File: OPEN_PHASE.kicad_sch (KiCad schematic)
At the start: 0 parts

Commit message: Rename the project to OPEN_PHASE
PhaseSense-8586 was named after the first parts of the design (INA240 +
ADS8586S), which are no longer on the board. OPEN_PHASE follows
OPEN_WEIGHT, the other OPEN THRUST LAB board.

- project files: OPEN_PHASE.kicad_pro / _sch / _pcb / _prl / _dru
- libraries: lib/lib_sym/OPEN_PHASE.kicad_sym and
  lib/lib_fp/OPEN_PHASE.pretty, nickname OPEN_PHASE in both tables, in
  every lib_id and in every footprint of the PCB
- project name of every symbol and sheet instance, so the reference
  designators are kept
- PROJECT_NAME and GIT_URL in the project and in kibot_main.yaml, README
  and its template, CHANGELOG, LTspice headers and their generator
- the README note now says the project was first published as
  PhaseSense-8586

The GitHub repository is now foukouda/OPEN_PHASE. The board name
PHASETRACKER is unchanged. The netlist, ERC and DRC reports are the same
before and after the rename.

Co-Authored-By: Claude Opus 5.5 <noreply@anthropic.com>
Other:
- title: PhaseSense-8586 - PHASETRACKER -> OPEN_PHASE - PHASETRACKER
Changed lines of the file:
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@@
 	(paper "A3")
 	(title_block
-		(title "PhaseSense-8586 - PHASETRACKER")
+		(title "OPEN_PHASE - PHASETRACKER")
 		(date "2026-10-06")
 		(rev "${REVISION}")
@@
 		)
 		(instances
-			(project "PhaseSense-8586"
+			(project "OPEN_PHASE"
 				(path "/f9e05184-c88b-4a88-ae9c-ab2bdb32be7c"
 					(page "9")
@@
 		)
 		(instances
-			(project "PhaseSense-8586"
+			(project "OPEN_PHASE"
 				(path "/f9e05184-c88b-4a88-ae9c-ab2bdb32be7c"
 					(page "10")
@@
 		)
 		(instances
-			(project "PhaseSense-8586"
+			(project "OPEN_PHASE"
 				(path "/f9e05184-c88b-4a88-ae9c-ab2bdb32be7c"
 					(page "2")
@@
 		)
 		(instances
-			(project "PhaseSense-8586"
+			(project "OPEN_PHASE"
 				(path "/f9e05184-c88b-4a88-ae9c-ab2bdb32be7c"
 					(page "3")

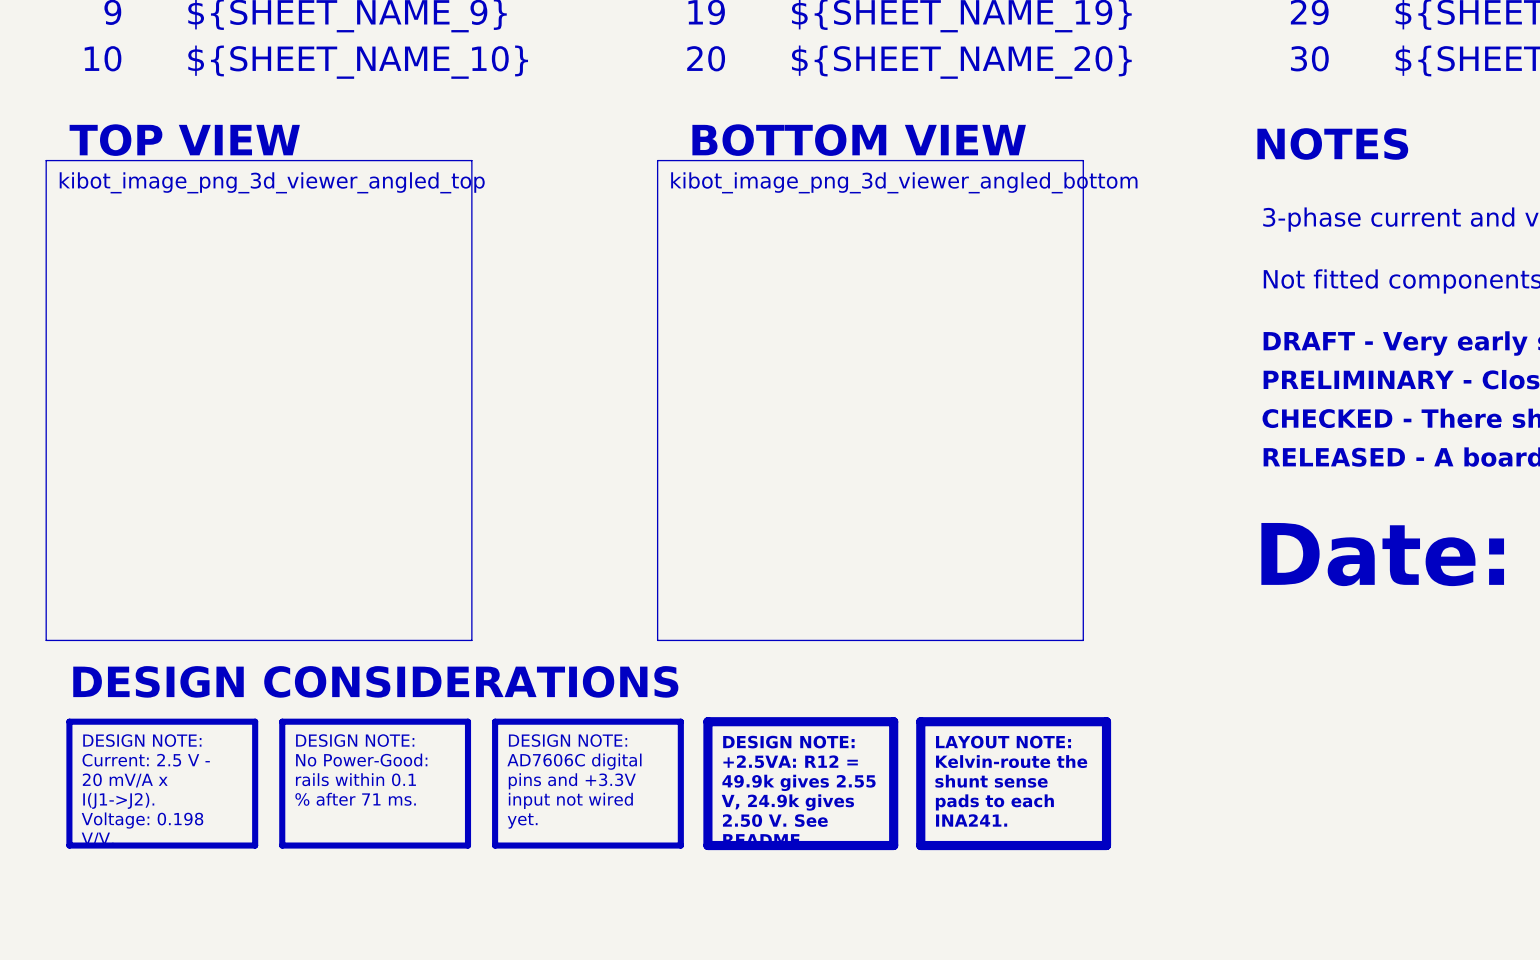
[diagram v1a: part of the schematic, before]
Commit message: Restyle schematic sheets, new title block logo, WE-MAPI inductor in simulations
- Schematic sheets: restyled frames, tables and text boxes
- Title block: INGENIERIE FRANCE logo in KDT_Template_GIT.kicad_wks
- LTspice: L1 modelled as WE-MAPI 4030 74438357022 (22 mOhm),
  simulations 01 and 03 rerun, README and results updated

Co-Authored-By: Claude Opus 5.5 <noreply@anthropic.com>
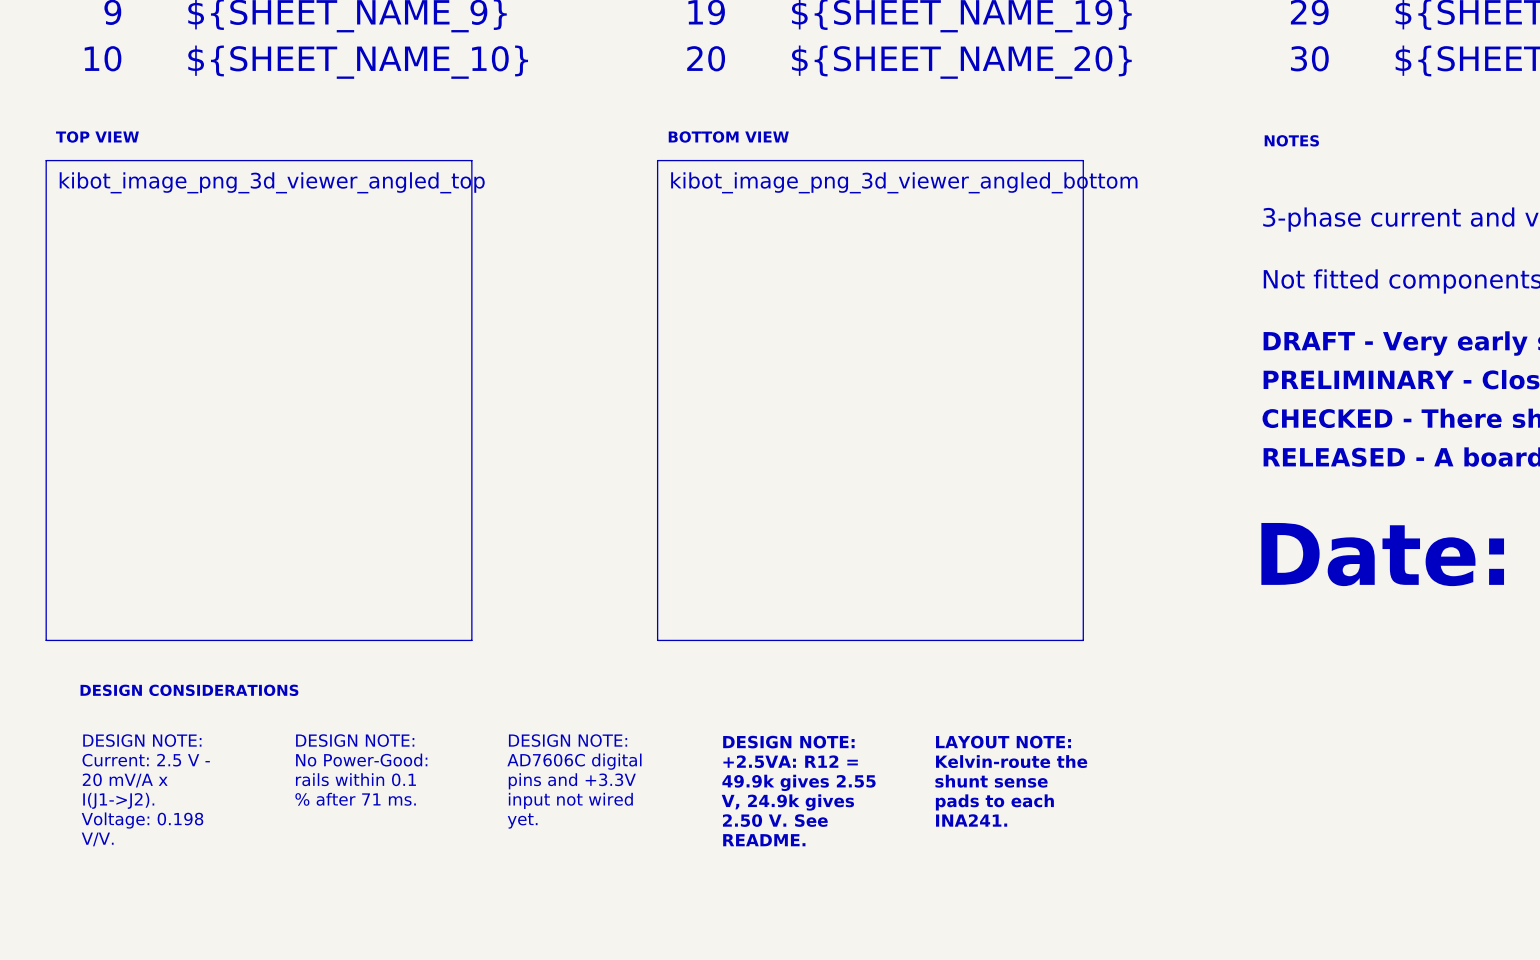
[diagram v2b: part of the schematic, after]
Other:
- note removed: "BOTTOM VIEW"
- note removed: "DESIGN CONSIDERATIONS"
- note removed: "NOTES"
- note removed: "TOP VIEW"
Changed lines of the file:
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@@
-		)
-	)
-	(text "BOTTOM VIEW"
-		(exclude_from_sim no)
-		(at 128.27 166.37 0)
-		(effects
-			(font
-				(face "Arial")
-				(size 5 5)
-				(bold yes)
-				(color 53 60 207 1)
-			)
-			(justify left bottom)
 		)
 	)
@@
 		)
 	)
-	(text "NOTES"
-		(exclude_from_sim no)
-		(at 220.98 167.005 0)
-		(effects
-			(font
-				(face "Arial")
-				(size 5 5)
-				(bold yes)
-				(color 53 60 207 1)
-			)
-			(justify left bottom)
-		)
-	)
 	(text "${SHEET_NAME_40}"
 		(exclude_from_sim no)
@@
 		)
 	)
-	(text "TOP VIEW"
-		(exclude_from_sim no)
-		(at 26.67 166.37 0)
-		(effects
-			(font
-				(face "Arial")
-				(size 5 5)
+	(text "34"
+		(exclude_from_sim no)
+		(at 332.74 106.68 0)
+		(effects
+			(font
+				(face "Times New Roman")
+				(size 4 4)
+				(color 0 0 0 1)
+			)
+			(justify right bottom)
+			(href "#34")
+		)
+	)
+	(text "${SHEET_NAME_10}"
+		(exclude_from_sim no)
+		(at 45.72 152.4 0)
+		(effects
+			(font
+				(face "Times New Roman")
+				(size 4 4)
+				(color 0 0 0 1)
+			)
+			(justify left bottom)
+			(href "#10")
+		)
+	)
+	(text "Index"
+		(exclude_from_sim no)
+		(at 45.72 71.12 0)
+		(effects
+			(font
+				(face "Times New Roman")
+				(size 4 4)
 				(bold yes)
-				(color 53 60 207 1)
-			)
-			(justify left bottom)
-		)
-	)
-	(text "34"
-		(exclude_from_sim no)
-		(at 332.74 106.68 0)
-		(effects
-			(font
-				(face "Times New Roman")
-				(size 4 4)
-				(color 0 0 0 1)
-			)
-			(justify right bottom)
-			(href "#34")
-		)
-	)
-	(text "${SHEET_NAME_10}"
-		(exclude_from_sim no)
-		(at 45.72 152.4 0)
-		(effects
-			(font
-				(face "Times New Roman")
-				(size 4 4)
-				(color 0 0 0 1)
-			)
-			(justify left bottom)
-			(href "#10")
-		)
-	)
-	(text "Index"
-		(exclude_from_sim no)
-		(at 45.72 71.12 0)
-		(effects
-			(font
-				(face "Times New Roman")
-				(size 4 4)
-				(bold yes)
 				(color 0 0 0 1)
 			)
@@
 			(justify left bottom)
 			(href "#25")
-		)
-	)
-	(text "DESIGN CONSIDERATIONS"
-		(exclude_from_sim no)
-		(at 26.67 255.27 0)
-		(effects
-			(font
-				(face "Arial")
-				(size 5 5)
-				(bold yes)
-				(color 53 60 207 1)
-			)
-			(justify left bottom)
 		)
 	)
@@
 		(margins 2 2 2 2)
 		(stroke
-			(width 1)
+			(width -0.0001)
 			(type solid)
-			(color 250 236 0 1)
-		)
-		(fill
-			(type none)
+		)
+		(fill
+			(type color)
+			(color 253 241 226 1)
 		)
 		(effects
@@
 		(margins 2 2 2 2)
 		(stroke
-			(width 1)
+			(width -0.0001)
 			(type solid)
-			(color 255 165 0 1)
-		)
-		(fill
-			(type none)
+		)
+		(fill
+			(type color)
+			(color 253 241 226 1)
 		)
 		(effects
@@
 		(margins 2.25 2.25 2.25 2.25)
 		(stroke
-			(width 1.5)
+			(width -0.0001)
 			(type solid)
-			(color 255 0 0 1)
-		)
-		(fill
-			(type none)
+		)
+		(fill
+			(type color)
+			(color 250 232 232 1)
 		)
 		(effects
@@
 		(margins 2.25 2.25 2.25 2.25)
 		(stroke
-			(width 1.5)
+			(width -0.0001)
 			(type solid)
-			(color 0 0 255 1)
-		)
-		(fill
-			(type none)
+		)
+		(fill
+			(type color)
+			(color 228 238 250 1)
 		)
 		(effects
@@
 		(margins 2 2 2 2)
 		(stroke
-			(width 1)
+			(width -0.0001)
 			(type solid)
-			(color 200 200 200 1)
-		)
-		(fill
-			(type none)
+		)
+		(fill
+			(type color)
+			(color 253 241 226 1)
 		)
 		(effects
@@
 		)
 	)
+	(text_box "TOP VIEW"
+		(exclude_from_sim no)
+		(at 22.86 159.39 0)
+		(size 69.85 6.35)
+		(margins 1.6 1.6 1.6 1.6)
+		(stroke
+			(width -0.0001)
+			(type solid)
+		)
+		(fill
+			(type color)
+			(color 162 22 34 1)
+		)
+		(effects
+			(font
+				(face "Arial")
+				(size 1.8 1.8)
+				(thickness 0.36)
+				(bold yes)
+				(color 255 255 255 1)
+			)
+			(justify left)
+		)
+	)
+	(text_box "BOTTOM VIEW"
+		(exclude_from_sim no)
+		(at 123.19 159.39 0)
+		(size 69.85 6.35)
+		(margins 1.6 1.6 1.6 1.6)
+		(stroke
+			(width -0.0001)
+			(type solid)
+		)
+		(fill
+			(type color)
+			(color 162 22 34 1)
+		)
+		(effects
+			(font
+				(face "Arial")
+				(size 1.8 1.8)
+				(thickness 0.36)
+				(bold yes)
+				(color 255 255 255 1)
+			)
+			(justify left)
+		)
+	)
+	(text_box "NOTES"
+		(exclude_from_sim no)
+		(at 220.98 160.02 0)
+		(size 180.34 6.35)
+		(margins 1.6 1.6 1.6 1.6)
+		(stroke
+			(width -0.0001)
+			(type solid)
+		)
+		(fill
+			(type color)
+			(color 0 105 120 1)
+		)
+		(effects
+			(font
+				(face "Arial")
+				(size 1.8 1.8)
+				(thickness 0.36)
+				(bold yes)
+				(color 255 255 255 1)
+			)
+			(justify left)
+		)
+	)
+	(text_box "DESIGN CONSIDERATIONS"
+		(exclude_from_sim no)
+		(at 26.67 250.19 0)
+		(size 170.18 6.35)
+		(margins 1.6 1.6 1.6 1.6)
+		(stroke
+			(width -0.0001)
+			(type solid)
+		)
+		(fill
+			(type color)
+			(color 205 100 0 1)
+		)
+		(effects
+			(font
+				(face "Arial")
+				(size 1.8 1.8)
+				(thickness 0.36)
+				(bold yes)
+				(color 255 255 255 1)
+			)
+			(justify left)
+		)
+	)
